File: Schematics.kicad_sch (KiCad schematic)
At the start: 53 parts, among them Q1 AO3400A, Q2 SI2301CDS-T1-E3, Q3 SI2301CDS-T1-E3, Q4 8050

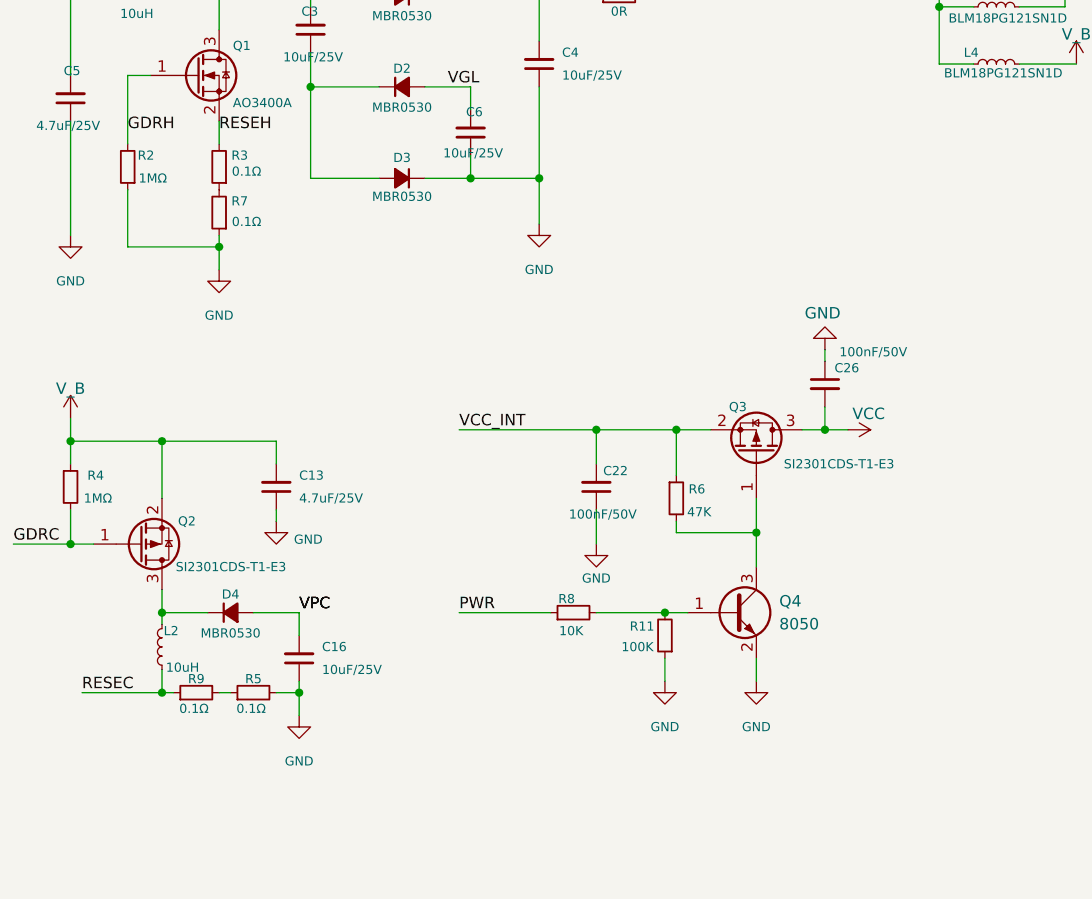
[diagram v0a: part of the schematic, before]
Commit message: added edge cuts and connected 2 unconnected ground pins
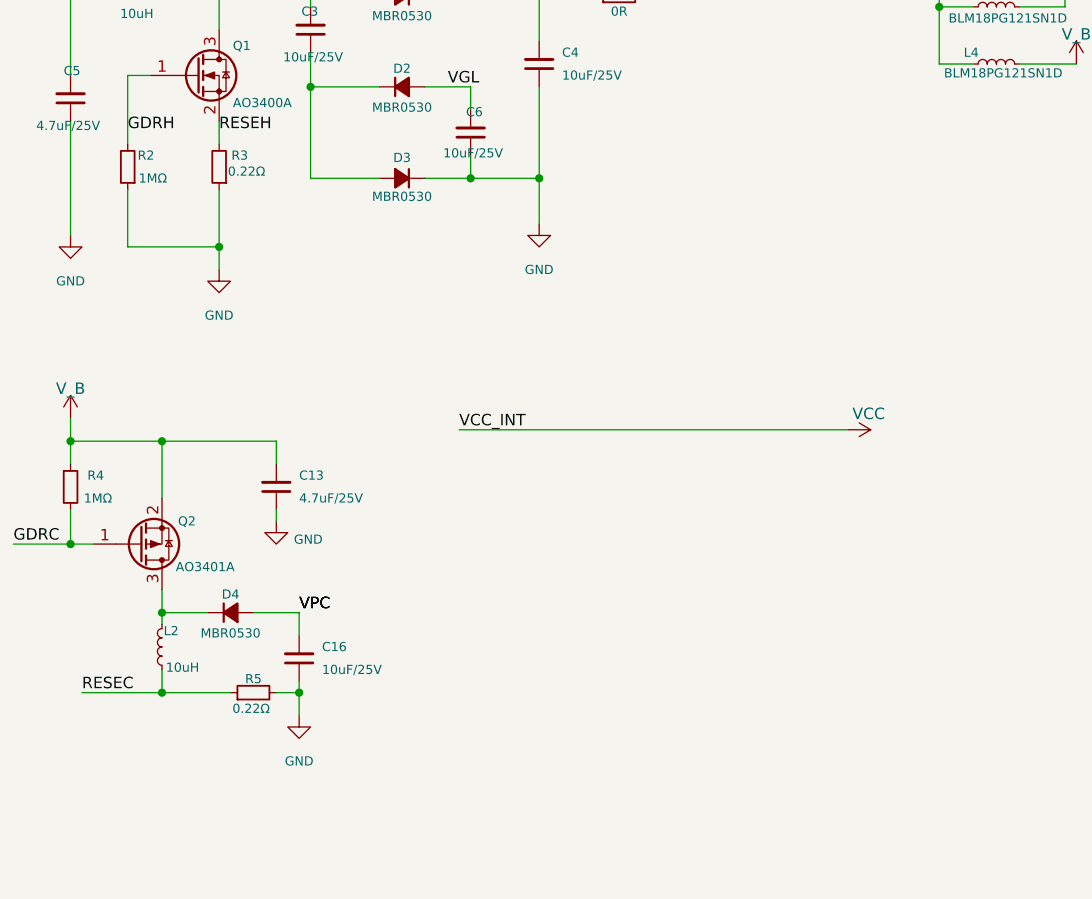
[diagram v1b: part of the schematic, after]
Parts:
- removed C22, C26: 100nF/50V, Capacitor_SMD:C_0603_1608Metric, symbol Device:C_Small
- removed Q3: SI2301CDS-T1-E3, local:SOT-23_L2.9-W1.3-P1.90-LS2.4-BR, symbol Transistor_FET:Q_PMOS_GSD
- removed Q4: 8050, local:SOT-23-3_L3.0-W1.7-P0.95-LS2.9-BR, symbol Transistor_BJT:SS8050
- removed R11: 100K, Resistor_SMD:R_0603_1608Metric, symbol Device:R_Small
- removed R6: 47K, Resistor_SMD:R_0603_1608Metric, symbol Device:R_Small
- removed R7, R9: 0.1Ω, Resistor_SMD:R_0603_1608Metric, symbol Device:R_Small
- removed R8: 10K, Resistor_SMD:R_0603_1608Metric, symbol Device:R_Small
- Q2: value SI2301CDS-T1-E3 -> AO3401A; footprint local:SOT-23_L2.9-W1.3-P1.90-LS2.4-BR -> local:SOT-23-3_L2.9-W1.3-P1.90-LS2.4-BR
- R3, R5: value 0.1Ω -> 0.22Ω; footprint Resistor_SMD:R_0603_1608Metric -> Resistor_SMD:R_0805_2012Metric
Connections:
- net VCC_INT is gone; now on net VCC: P2.1
- net GND: now also R3.1
- net RESEC: now also R5.1
